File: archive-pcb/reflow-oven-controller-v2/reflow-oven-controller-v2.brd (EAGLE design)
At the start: 76.2 x 50.5 mm, 17 parts, among them IC1 MAX6675

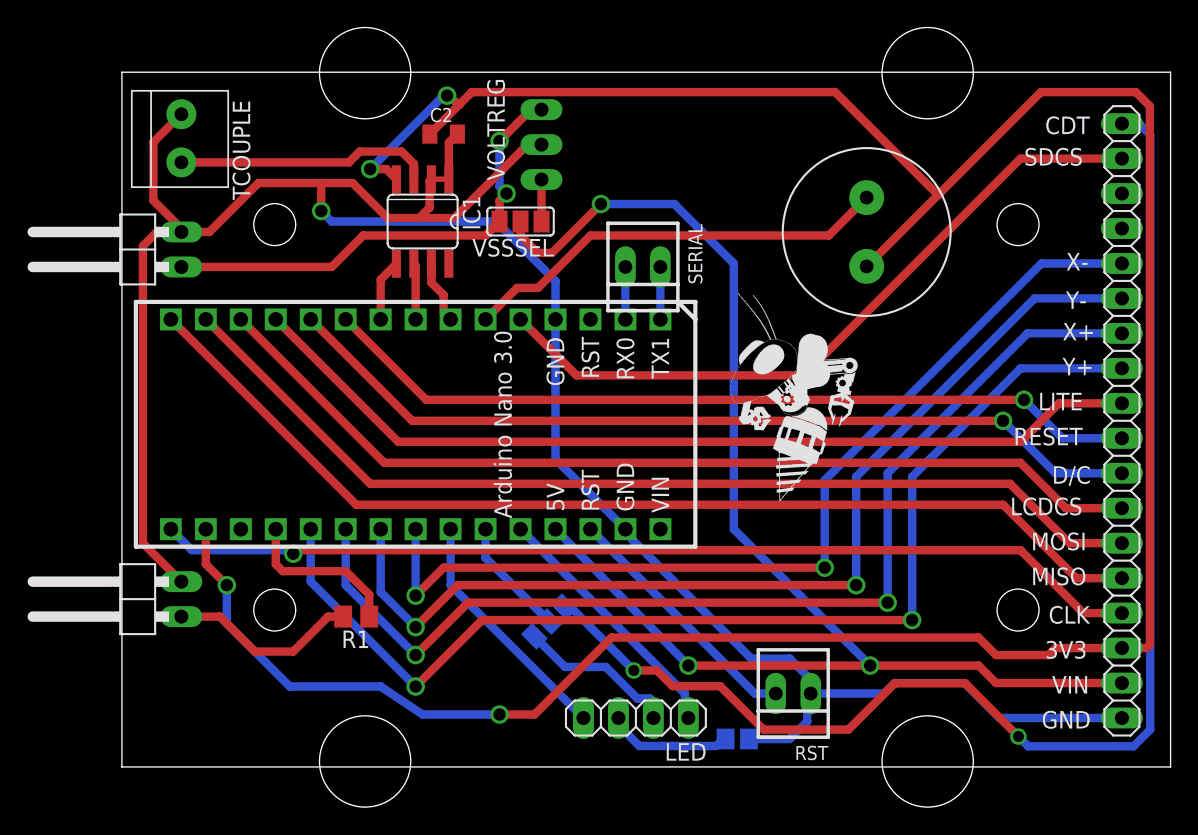
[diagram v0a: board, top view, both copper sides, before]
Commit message: updating reflow board with ground plane
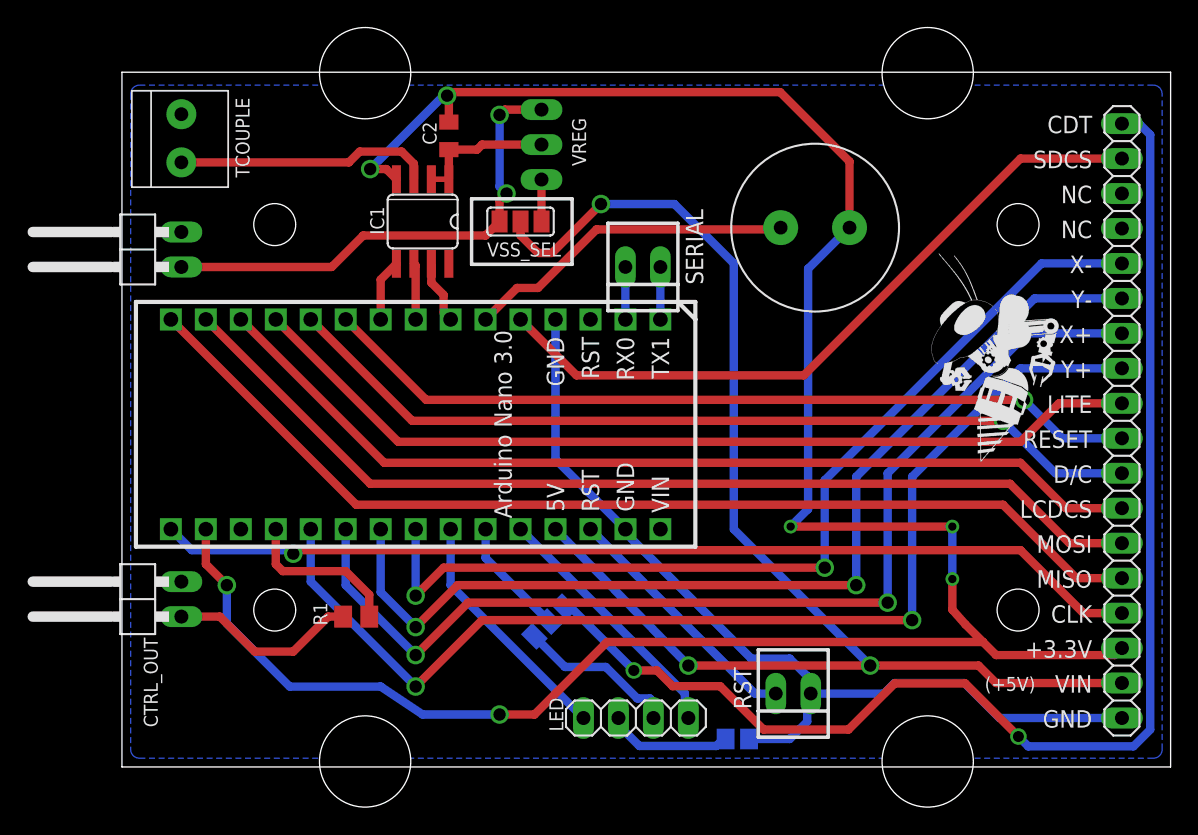
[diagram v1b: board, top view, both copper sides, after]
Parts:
- JP1: value Relay Signal -> CTRL_OUT
- JP2: value 5VIN -> VIN
- moved U$2 14.9 mm to (62.4, 22.2)
- moved SP1 3.76 mm to (50.4, 39.2), turned to 0 degrees
- moved C2 0.40 mm to (23.7, 45.8), turned to 270 degrees
- renumbered VOLTREG to VREG, VSSSEL to VSS_SEL
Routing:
- net GND: track 169.3 -> 77.8 mm, vias 1 -> 0
- net VSS: track 198.0 -> 170.8 mm, vias 4 -> 7
- net SPK: track 31.4 -> 24.3 mm
- net TRANSIN: track 34.7 -> 36.6 mm
- added copper zone on layer 16, net GND
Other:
- board text added: "(+5V)"
- board text added: "+3.3V"
- board text added: "NC"
- board text removed: "3V3"
